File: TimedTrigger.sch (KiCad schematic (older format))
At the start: 93 parts, among them J1 9V_JACK, J10 TRESH_PHNX, J11 TRIGGER_3.5mm, J12 Trigger_PHNX, J2 PWR_IN_PHNX, J3 OUT1_PHNX, J4 OUT1_3.5mm, J5 OUT2_PHNX, J6 OUT2_3.5mm, J7 OUT2_PHNX, J8 OUT2_3.5mm, J9 THRESH_3.5mm, Q1 2N3904, Q2 2N3904, Q3 2N3904, SW1 SW_SPDT, SW2 RETRIG_MODE, SW3 Manual_Trigger, U1 LM324, U2 NA555, U3 LM358, U4 NA555, U5 NA555, U6 LM358, U7 LM358, U8 LM358

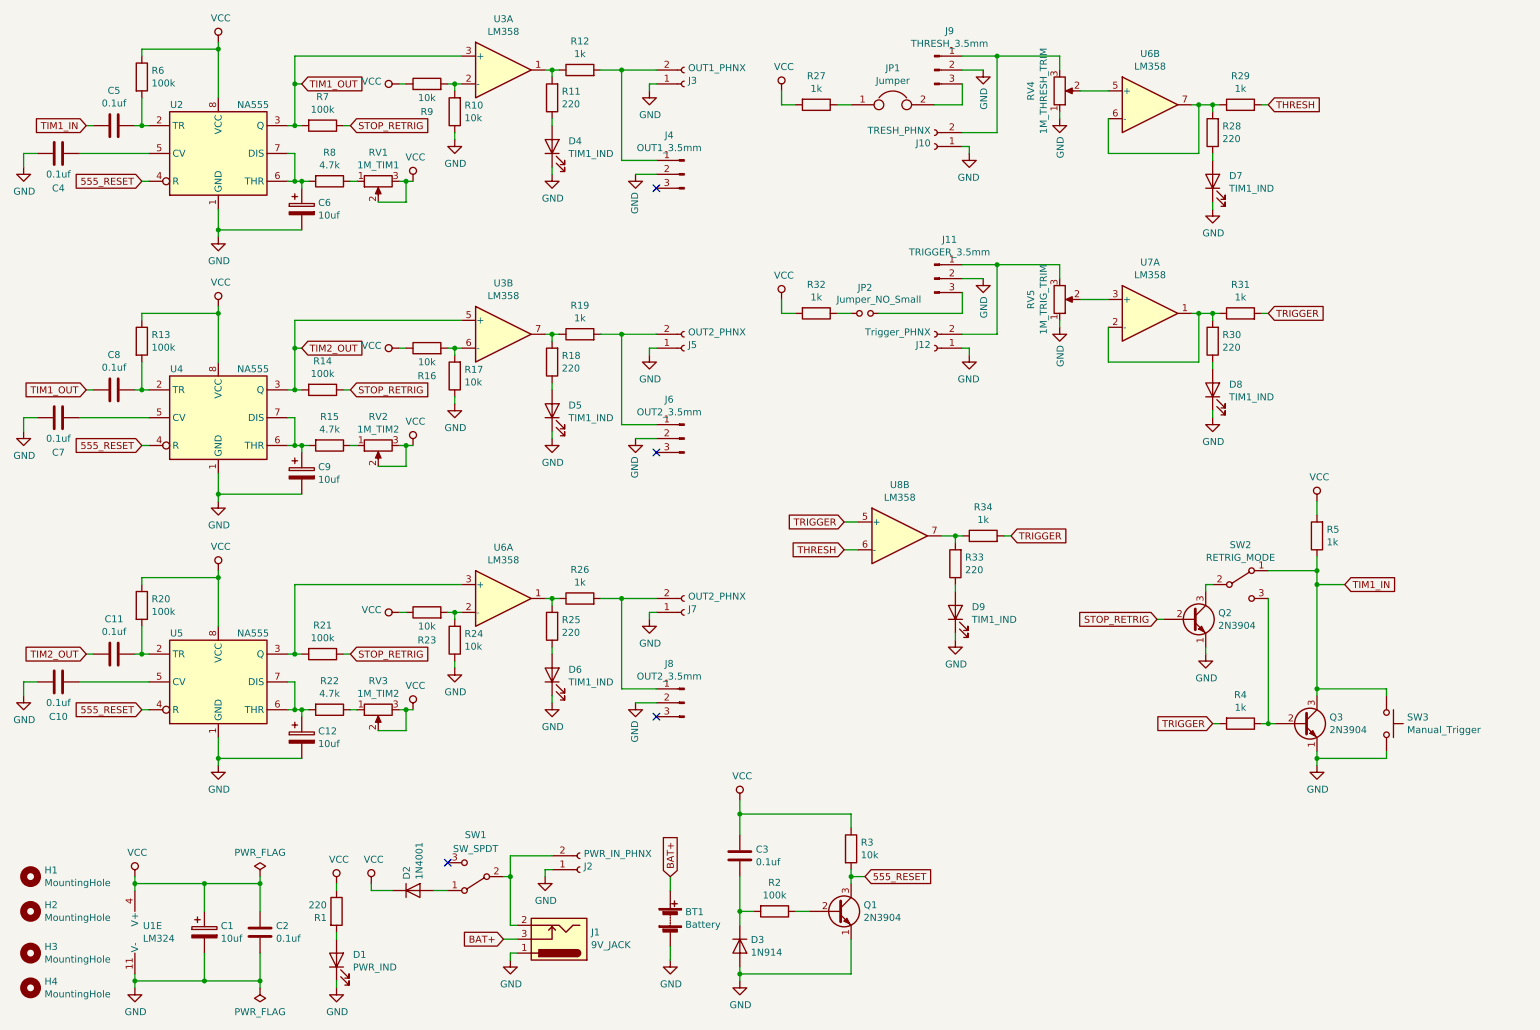
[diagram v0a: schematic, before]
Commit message: added components
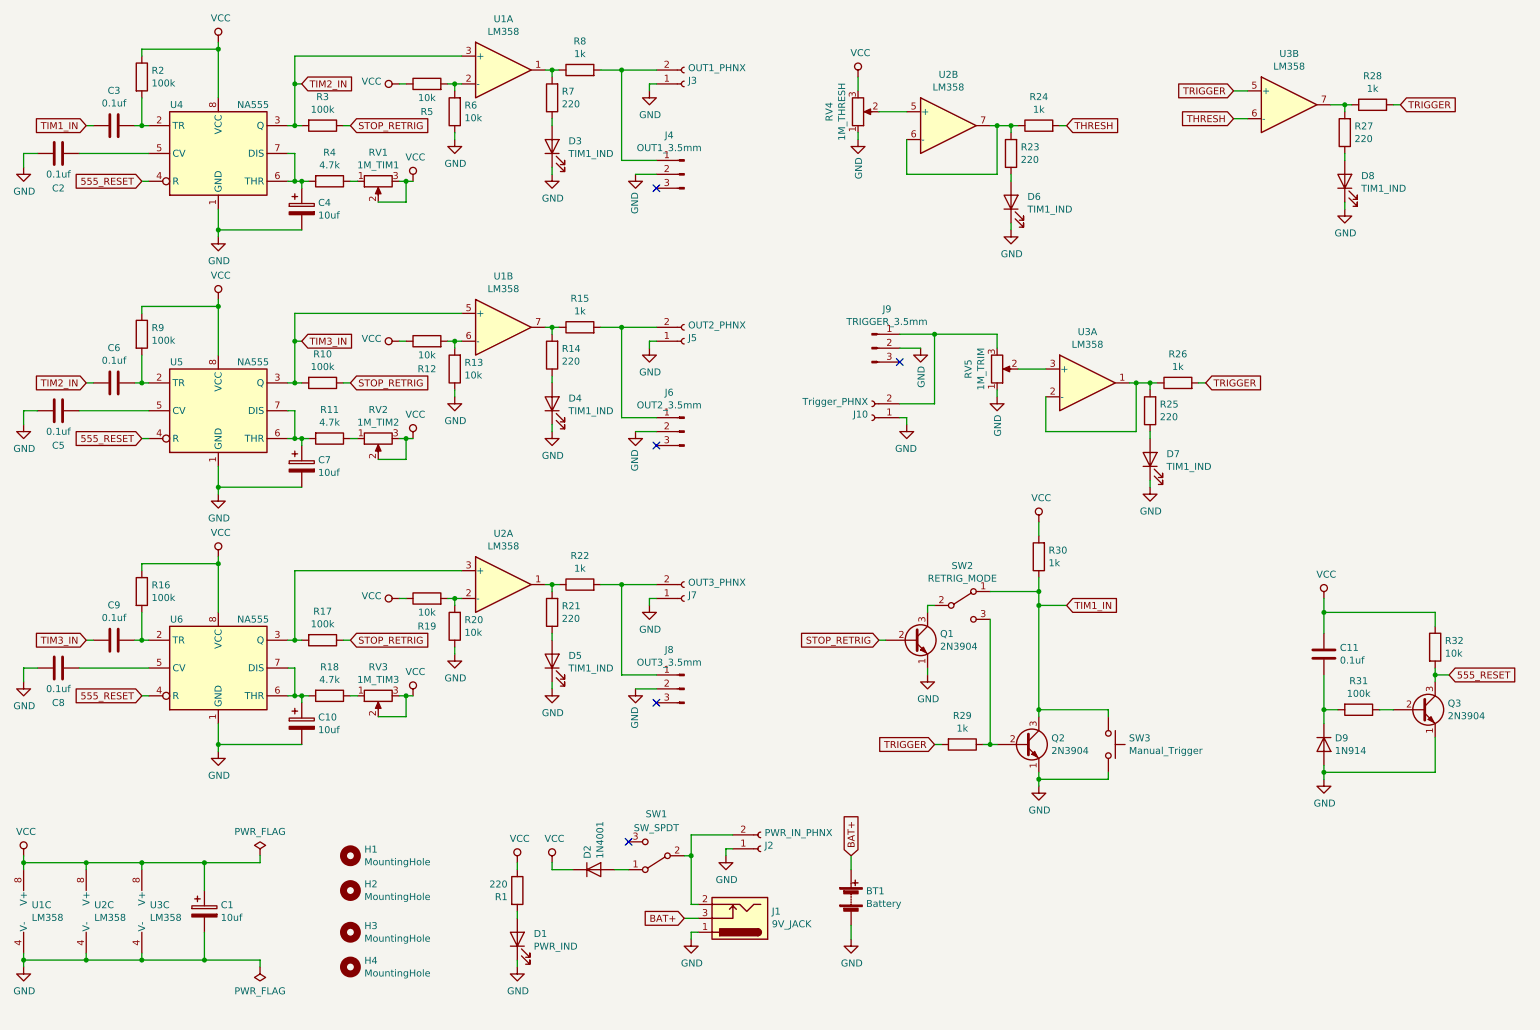
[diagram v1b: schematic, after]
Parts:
- removed C2: 0.1uf, Capacitor_THT:C_Disc_D3.0mm_W2.0mm_P2.50mm, symbol Device:C
- removed J10: TRESH_PHNX, Connector_Phoenix_MC:PhoenixContact_MC_1,5_2-G-3.81_1x02_P3.81mm_Horizontal, symbol Connector:Conn_01x02_Female
- removed J9: THRESH_3.5mm, HammerheadAudio:EuroJack_MonoSW_THT, symbol Connector:Conn_01x03_Male
- removed JP1: Jumper, Jumper:SolderJumper-2_P1.3mm_Bridged_Pad1.0x1.5mm, symbol Device:Jumper
- removed JP2: Jumper_NO_Small, Jumper:SolderJumper-2_P1.3mm_Open_Pad1.0x1.5mm, symbol Device:Jumper_NO_Small
- removed R27, R32: 1k, HammerheadAudio:R_THT_P7.62, symbol Device:R
- removed U1: LM324, Package_DIP:DIP-14_W7.62mm_Socket, symbol Amplifier_Operational:LM324
- added unit 3 of U1
- added unit 3 of U2
- added unit 3 of U3
- J7: value OUT2_PHNX -> OUT3_PHNX
- J8: value OUT2_3.5mm -> OUT3_3.5mm
- RV3: value 1M_TIM2 -> 1M_TIM3
- RV4: value 1M_THRESH_TRIM -> 1M_THRESH
- RV5: value 1M_TRIG_TRIM -> 1M_TRIM
- renumbered C12 to C10, C3 to C11, C4 to C2, C5 to C3, C6 to C4, C7 to C5, C8 to C6, C9 to C7, C10 to C8, C11 to C9, D4 to D3, D5 to D4, D6 to D5, D7 to D6, D8 to D7, D9 to D8, D3 to D9, J12 to J10, J11 to J9, Q2 to Q1, Q3 to Q2, Q1 to Q3, R14 to R10, R15 to R11, R16 to R12, R17 to R13, R18 to R14, R19 to R15, R20 to R16, R21 to R17, R22 to R18, R23 to R19, R6 to R2, R24 to R20, R25 to R21, R26 to R22, R28 to R23, R29 to R24, R30 to R25, R31 to R26, R33 to R27, R34 to R28, R4 to R29, R7 to R3, R5 to R30, R2 to R31, R3 to R32, R8 to R4, R9 to R5, R10 to R6, R11 to R7, R12 to R8, R13 to R9, U3 to U1, U6 to U2, U7 to U3, U8 to U3, U2 to U4, U4 to U5, U5 to U6
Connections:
- net GND: now also U1.4 (V-), U2.4 (V-), U3.4 (V-)
- net VCC: now also RV4.3, U1.8 (V+), U2.8 (V+), U3.8 (V+)
- net TIM1_OUT renamed TIM2_IN
- net TIM2_OUT renamed TIM3_IN
- no-connect marks 4 -> 5
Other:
- moved on the sheet: BT1, C1, C10, C11, C5, C6, C7, C8, C9, D1, D2, D4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

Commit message: Started laying out components
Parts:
- D4: value TIM1_IND -> TIM2_IND
- D5: value TIM1_IND -> TIM3_IND
- D6: value TIM1_IND -> THRESH_IND
- D7: value TIM1_IND -> INPUT_IND
- D8: value TIM1_IND -> TRIG_IND
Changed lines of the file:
@@
 P 4400 5200
 F 0 "D5" V 4439 5082 50  0000 R CNN
-F 1 "TIM1_IND" V 4348 5082 50  0000 R CNN
+F 1 "TIM3_IND" V 4348 5082 50  0000 R CNN
 F 2 "LED_THT:LED_D5.0mm" H 4400 5200 50  0001 C CNN
 F 3 "~" H 4400 5200 50  0001 C CNN
@@
 P 10100 1750
 F 0 "D8" V 10139 1632 50  0000 R CNN
-F 1 "TIM1_IND" V 10048 1632 50  0000 R CNN
+F 1 "TRIG_IND" V 10048 1632 50  0000 R CNN
 F 2 "LED_THT:LED_D5.0mm" H 10100 1750 50  0001 C CNN
 F 3 "~" H 10100 1750 50  0001 C CNN
@@
 P 8700 3750
 F 0 "D7" V 8739 3632 50  0000 R CNN
-F 1 "TIM1_IND" V 8648 3632 50  0000 R CNN
+F 1 "INPUT_IND" V 8648 3632 50  0000 R CNN
 F 2 "LED_THT:LED_D5.0mm" H 8700 3750 50  0001 C CNN
 F 3 "~" H 8700 3750 50  0001 C CNN
@@
 P 7700 1900
 F 0 "D6" V 7739 1782 50  0000 R CNN
-F 1 "TIM1_IND" V 7648 1782 50  0000 R CNN
+F 1 "THRESH_IND" V 7648 1782 50  0000 R CNN
 F 2 "LED_THT:LED_D5.0mm" H 7700 1900 50  0001 C CNN
 F 3 "~" H 7700 1900 50  0001 C CNN
@@
 P 4400 3350
 F 0 "D4" V 4439 3232 50  0000 R CNN
-F 1 "TIM1_IND" V 4348 3232 50  0000 R CNN
+F 1 "TIM2_IND" V 4348 3232 50  0000 R CNN
 F 2 "LED_THT:LED_D5.0mm" H 4400 3350 50  0001 C CNN
 F 3 "~" H 4400 3350 50  0001 C CNN
